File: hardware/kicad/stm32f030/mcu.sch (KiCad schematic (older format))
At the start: 13 parts, among them P10 SWD, P8 UART, P9 I2C, SW3 RESET, U2 STM32F030F4Px, Y1 8MHz

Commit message: hardware/kicad/stm32f030: progress
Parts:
- removed JP3: JP3x1, Pin_Headers:Pin_Header_Straight_1x03_Pitch2.54mm, symbol JP3x1
- added JP3: boot0, Pin_Headers:Pin_Header_Straight_1x02_Pitch2.54mm, symbol Jumper_NO_Small
- added R28: 10k, Resistors_SMD:R_0603_HandSoldering, symbol R_Small
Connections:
- net labels added: RXD, SWC, SWD, TXD
- wire segments 48 -> 53
- no-connect marks 0 -> 3
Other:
- moved on the sheet: C16, P10, P8, P9, R25, R26, SW3

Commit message: hardware/kicad/stm32f030: progress
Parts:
- U2: footprint Housings_SSOP:TSSOP-20_4.4x6.5mm_Pitch0.65mm -> Housings_SSOP:TSSOP-20_4.4x6.5mm_Pitch0.65mm_Handsoldering
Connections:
- net GND: now also SW3.1; no longer SW3.2
- net reset: now also SW3.2; no longer SW3.1
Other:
- moved on the sheet: C16
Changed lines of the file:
@@
 F 0 "U2" H 4450 4675 50  0000 L BNN
 F 1 "STM32F030F4Px" H 7650 4675 50  0000 R BNN
-F 2 "Housings_SSOP:TSSOP-20_4.4x6.5mm_Pitch0.65mm" H 7650 4625 50  0001 R TNN
+F 2 "Housings_SSOP:TSSOP-20_4.4x6.5mm_Pitch0.65mm_Handsoldering" H 7650 4625 50  0001 R TNN
 F 3 "" H 6050 3750 50  0000 C CNN
 	1    6050 3750
@@
 L +3.3V #PWR044
 U 1 1 5884CB05
-P 8800 4600
-F 0 "#PWR044" H 8800 4450 50  0001 C CNN
-F 1 "+3.3V" H 8800 4740 50  0000 C CNN
-F 2 "" H 8800 4600 50  0000 C CNN
-F 3 "" H 8800 4600 50  0000 C CNN
-	1    8800 4600
+P 8800 4500
+F 0 "#PWR044" H 8800 4350 50  0001 C CNN
+F 1 "+3.3V" H 8800 4640 50  0000 C CNN
+F 2 "" H 8800 4500 50  0000 C CNN
+F 3 "" H 8800 4500 50  0000 C CNN
+	1    8800 4500
 	1    0    0    -1
 $EndComp
@@
 L C_Small C16
 U 1 1 5884CB14
-P 8800 4750
-F 0 "C16" H 8810 4820 50  0000 L CNN
-F 1 "100n" H 8810 4670 50  0000 L CNN
-F 2 "Capacitors_SMD:C_0805_HandSoldering" H 8800 4750 50  0001 C CNN
-F 3 "" H 8800 4750 50  0000 C CNN
-	1    8800 4750
+P 8800 4700
+F 0 "C16" H 8810 4770 50  0000 L CNN
+F 1 "100n" H 8810 4620 50  0000 L CNN
+F 2 "Capacitors_SMD:C_0805_HandSoldering" H 8800 4700 50  0001 C CNN
+F 3 "" H 8800 4700 50  0000 C CNN
+	1    8800 4700
 	1    0    0    -1
 $EndComp
@@
 F 3 "" H 8600 3150 50  0000 C CNN
 	1    8600 3150
-	1    0    0    -1
+	-1   0    0    -1
 $EndComp
 $Comp
@@
 NoConn ~ 4350 3550
 Wire Wire Line
-	6050 2600 6050 2750
+	6050 2600 6050 2650
+Wire Wire Line
+	6050 2650 6050 2750
 Wire Wire Line
 	6150 2750 6150 2650
@@
 Connection ~ 6050 2650
 Wire Wire Line
-	6050 4650 6050 4900
-Wire Wire Line
-	8800 4600 8800 4650
-Wire Wire Line
-	8800 4850 8800 4900
+	8800 4500 8800 4600
+Wire Wire Line
+	8800 4800 8800 4900
 Wire Wire Line
 	7750 4250 9450 4250
 Wire Wire Line
-	7750 3150 8400 3150
-Wire Wire Line
-	8800 3150 8950 3150
+	7750 3150 7950 3150
+Wire Wire Line
+	7950 3150 8350 3150
+Wire Wire Line
+	8350 3150 8400 3150
 Wire Wire Line
 	8950 3150 8950 3250
 Wire Wire Line
-	7950 2950 7950 4150
+	7950 2950 7950 3150
+Wire Wire Line
+	7950 3150 7950 4150
 Connection ~ 7950 3150
 Wire Wire Line
 	7950 2600 7950 2750
 Wire Wire Line
-	3950 3550 3950 4900
+	3950 3550 3950 3950
+Wire Wire Line
+	3950 3950 3950 4600
+Wire Wire Line
+	3950 4600 3950 4900
 Wire Wire Line
 	3950 4600 3900 4600
@@
 	3900 3550 3950 3550
 Wire Wire Line
-	7850 4050 7850 4600
+	7850 4050 7850 4450
+Wire Wire Line
+	7850 4450 7850 4600
 Wire Wire Line
 	7850 4050 7750 4050
 Wire Wire Line
-	8150 3950 8150 4600
+	8150 3950 8150 4450
+Wire Wire Line
+	8150 4450 8150 4600
 Wire Wire Line
 	8150 3950 7750 3950
@@
 	3050 3000 4250 3000
 Wire Wire Line
-	4250 2850 4250 4050
-Wire Wire Line
-	4050 2850 4050 4050
+	4250 2850 4250 3000
+Wire Wire Line
+	4250 3000 4250 4050
+Wire Wire Line
+	4050 2850 4050 3100
+Wire Wire Line
+	4050 3100 4050 3950
+Wire Wire Line
+	4050 3950 4050 4050
 Connection ~ 4050 3100
 Connection ~ 4250 3000
@@
 	4050 4050 3900 4050
 Wire Wire Line
-	4150 4050 4350 4050
+	4150 4050 4250 4050
+Wire Wire Line
+	4250 4050 4350 4050
 Wire Wire Line
 	4150 4050 4150 4150
@@
 	8550 3750 8550 4300
 Wire Wire Line
-	8550 4500 8550 4600
+	8550 4500 8550 4550
+Wire Wire Line
+	8550 4550 8550 4600
 Wire Wire Line
 	8550 4900 8550 4800
@@
 Text Label 4000 4500 0    60   ~ 0
 SWD
+Wire Wire Line
+	8800 3150 8850 3150
+Wire Wire Line
+	8850 3150 8950 3150
+Wire Wire Line
+	8400 3250 8350 3250
+Wire Wire Line
+	8350 3250 8350 3150
+Connection ~ 8350 3150
+Wire Wire Line
+	8800 3250 8850 3250
+Wire Wire Line
+	8850 3250 8850 3150
+Connection ~ 8850 3150
+Wire Wire Line
+	6050 4900 6050 4650
 $EndSCHEMATC

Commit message: hardware/kicad/stm32f030: modules ready
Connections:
- net RXD: now also P8.1 (P1); no longer P8.2 (P2)
- net TXD: now also P8.2 (P2); no longer P8.1 (P1)
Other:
- moved on the sheet: P8
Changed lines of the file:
@@
 L CONN_01X03 P8
 U 1 1 5884E804
-P 3700 3450
-F 0 "P8" H 3700 3650 50  0000 C CNN
-F 1 "UART" V 3800 3450 50  0000 C CNN
-F 2 "Pin_Headers:Pin_Header_Straight_1x03_Pitch2.54mm" H 3700 3450 50  0001 C CNN
-F 3 "" H 3700 3450 50  0000 C CNN
-	1    3700 3450
-	-1   0    0    -1
+P 3700 3350
+F 0 "P8" H 3700 3550 50  0000 C CNN
+F 1 "UART" V 3800 3350 50  0000 C CNN
+F 2 "Pin_Headers:Pin_Header_Straight_1x03_Pitch2.54mm" H 3700 3350 50  0001 C CNN
+F 3 "" H 3700 3350 50  0000 C CNN
+	1    3700 3350
+	-1   0    0    1
 $EndComp
 Text HLabel 3050 3100 0    60   Output ~ 0
@@
 NoConn ~ 4350 3250
 NoConn ~ 4350 3550
-Wire Wire Line
-	6050 2600 6050 2650
-Wire Wire Line
-	6050 2650 6050 2750
-Wire Wire Line
-	6150 2750 6150 2650
-Wire Wire Line
-	6150 2650 6050 2650
-Connection ~ 6050 2650
-Wire Wire Line
-	8800 4500 8800 4600
-Wire Wire Line
-	8800 4800 8800 4900
-Wire Wire Line
-	7750 4250 9450 4250
-Wire Wire Line
-	7750 3150 7950 3150
-Wire Wire Line
-	7950 3150 8350 3150
-Wire Wire Line
-	8350 3150 8400 3150
-Wire Wire Line
-	8950 3150 8950 3250
-Wire Wire Line
-	7950 2950 7950 3150
-Wire Wire Line
-	7950 3150 7950 4150
-Connection ~ 7950 3150
-Wire Wire Line
-	7950 2600 7950 2750
-Wire Wire Line
-	3950 3550 3950 3950
-Wire Wire Line
-	3950 3950 3950 4600
-Wire Wire Line
-	3950 4600 3950 4900
-Wire Wire Line
-	3950 4600 3900 4600
-Connection ~ 3950 4600
-Wire Wire Line
-	3900 3550 3950 3550
-Wire Wire Line
-	7850 4050 7850 4450
-Wire Wire Line
-	7850 4450 7850 4600
-Wire Wire Line
-	7850 4050 7750 4050
-Wire Wire Line
-	8150 3950 8150 4450
-Wire Wire Line
-	8150 4450 8150 4600
-Wire Wire Line
-	8150 3950 7750 3950
-Wire Wire Line
-	7900 4450 7850 4450
-Connection ~ 7850 4450
-Wire Wire Line
-	8100 4450 8150 4450
-Connection ~ 8150 4450
-Wire Wire Line
-	8150 4900 8150 4800
-Wire Wire Line
-	7850 4900 7850 4800
-Wire Wire Line
-	4250 4150 4350 4150
-Wire Wire Line
-	4300 4250 4350 4250
-Wire Wire Line
-	3050 3850 4350 3850
-Wire Wire Line
-	3050 3750 4350 3750
-Wire Wire Line
-	3050 3650 4350 3650
-Wire Wire Line
-	3900 3450 4350 3450
-Wire Wire Line
-	3900 3350 4350 3350
-Wire Wire Line
-	7950 4150 9450 4150
-Wire Wire Line
-	3050 3100 4050 3100
-Connection ~ 4050 3950
-Wire Wire Line
-	3050 3000 4250 3000
-Wire Wire Line
-	4250 2850 4250 3000
-Wire Wire Line
-	4250 3000 4250 4050
-Wire Wire Line
-	4050 2850 4050 3100
-Wire Wire Line
-	4050 3100 4050 3950
-Wire Wire Line
-	4050 3950 4050 4050
-Connection ~ 4050 3100
-Connection ~ 4250 3000
-Wire Wire Line
-	4050 2600 4050 2650
-Wire Wire Line
-	4250 2600 4250 2650
-Wire Wire Line
-	4250 4150 4250 4500
-Wire Wire Line
-	4250 4500 3900 4500
-Wire Wire Line
-	3900 4400 4300 4400
-Wire Wire Line
-	4300 4400 4300 4250
-Wire Wire Line
-	4050 3950 4350 3950
-Wire Wire Line
-	3900 3950 3950 3950
-Connection ~ 3950 3950
-Wire Wire Line
-	4050 4050 3900 4050
-Wire Wire Line
-	4150 4050 4250 4050
-Wire Wire Line
-	4250 4050 4350 4050
-Wire Wire Line
-	4150 4050 4150 4150
-Wire Wire Line
-	4150 4150 3900 4150
-Connection ~ 4250 4050
 $Comp
 L R_Small R28
@@
 	0    1    1    0
 $EndComp
-Wire Wire Line
-	8550 3750 8550 4300
-Wire Wire Line
-	8550 4500 8550 4550
-Wire Wire Line
-	8550 4550 8550 4600
-Wire Wire Line
-	8550 4900 8550 4800
-Wire Wire Line
-	8550 4550 8350 4550
-Wire Wire Line
-	8350 4550 8350 3350
-Wire Wire Line
-	8350 3350 7750 3350
-Connection ~ 8550 4550
-Text Label 3950 3350 0    60   ~ 0
-TXD
-Text Label 3950 3450 0    60   ~ 0
+Text Label 4000 3450 0    60   ~ 0
 RXD
 Text Label 4000 4400 0    60   ~ 0
@@
 SWD
 Wire Wire Line
-	8800 3150 8850 3150
-Wire Wire Line
-	8850 3150 8950 3150
+	6050 2600 6050 2750
+Wire Wire Line
+	6150 2750 6150 2650
+Wire Wire Line
+	6150 2650 6050 2650
+Connection ~ 6050 2650
+Wire Wire Line
+	8800 4500 8800 4600
+Wire Wire Line
+	8800 4800 8800 4900
+Wire Wire Line
+	7750 4250 9450 4250
+Wire Wire Line
+	7750 3150 8400 3150
+Wire Wire Line
+	8950 3150 8950 3250
+Wire Wire Line
+	7950 2950 7950 4150
+Connection ~ 7950 3150
+Wire Wire Line
+	7950 2600 7950 2750
+Wire Wire Line
+	3950 4600 3900 4600
+Connection ~ 3950 4600
+Wire Wire Line
+	7850 4050 7850 4600
+Wire Wire Line
+	7850 4050 7750 4050
+Wire Wire Line
+	8150 3950 8150 4600
+Wire Wire Line
+	8150 3950 7750 3950
+Wire Wire Line
+	7900 4450 7850 4450
+Connection ~ 7850 4450
+Wire Wire Line
+	8100 4450 8150 4450
+Connection ~ 8150 4450
+Wire Wire Line
+	8150 4900 8150 4800
+Wire Wire Line
+	7850 4900 7850 4800
+Wire Wire Line
+	4250 4150 4350 4150
+Wire Wire Line
+	4300 4250 4350 4250
+Wire Wire Line
+	3050 3850 4350 3850
+Wire Wire Line
+	3050 3750 4350 3750
+Wire Wire Line
+	3050 3650 4350 3650
+Wire Wire Line
+	7950 4150 9450 4150
+Wire Wire Line
+	3050 3100 4050 3100
+Connection ~ 4050 3950
+Wire Wire Line
+	3050 3000 4250 3000
+Wire Wire Line
+	4250 2850 4250 4050
+Wire Wire Line
+	4050 2850 4050 4050
+Connection ~ 4050 3100
+Connection ~ 4250 3000
+Wire Wire Line
+	4050 2600 4050 2650
+Wire Wire Line
+	4250 2600 4250 2650
+Wire Wire Line
+	4250 4150 4250 4500
+Wire Wire Line
+	4250 4500 3900 4500
+Wire Wire Line
+	3900 4400 4300 4400
+Wire Wire Line
+	4300 4400 4300 4250
+Wire Wire Line
+	4050 3950 4350 3950
+Wire Wire Line
+	3900 3950 3950 3950
+Connection ~ 3950 3950
+Wire Wire Line
+	4050 4050 3900 4050
+Wire Wire Line
+	4150 4050 4350 4050
+Wire Wire Line
+	4150 4050 4150 4150
+Wire Wire Line
+	4150 4150 3900 4150
+Connection ~ 4250 4050
+Wire Wire Line
+	8550 3750 8550 4300
+Wire Wire Line
+	8550 4500 8550 4600
+Wire Wire Line
+	8550 4900 8550 4800
+Wire Wire Line
+	8550 4550 8350 4550
+Wire Wire Line
+	8350 4550 8350 3350
+Wire Wire Line
+	8350 3350 7750 3350
+Connection ~ 8550 4550
+Wire Wire Line
+	8800 3150 8950 3150
 Wire Wire Line
 	8400 3250 8350 3250
@@
 Wire Wire Line
 	6050 4900 6050 4650
+Wire Wire Line
+	3900 3350 4350 3350
+Wire Wire Line
+	3950 3250 3950 4900
+Wire Wire Line
+	3200 4750 3950 4750
+Connection ~ 3950 4750
+Wire Wire Line
+	3950 3250 3900 3250
+Wire Wire Line
+	3900 3450 4350 3450
+Text Label 4000 3350 0    60   ~ 0
+TXD
 $EndSCHEMATC

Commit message: PCB V0.90
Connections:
- net SWC: now also P10.2 (P2); no longer P10.1 (P1)
- net SWD: now also P10.1 (P1); no longer P10.2 (P2)
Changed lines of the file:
@@
 Text Label 4000 3450 0    60   ~ 0
 RXD
+Text Label 4000 4500 0    60   ~ 0
+SWC
 Text Label 4000 4400 0    60   ~ 0
-SWC
-Text Label 4000 4500 0    60   ~ 0
 SWD
 Wire Wire Line
@@
 	7850 4900 7850 4800
 Wire Wire Line
-	4250 4150 4350 4150
-Wire Wire Line
 	4300 4250 4350 4250
 Wire Wire Line
@@
 Wire Wire Line
 	4250 2600 4250 2650
-Wire Wire Line
-	4250 4150 4250 4500
-Wire Wire Line
-	4250 4500 3900 4500
-Wire Wire Line
-	3900 4400 4300 4400
-Wire Wire Line
-	4300 4400 4300 4250
 Wire Wire Line
 	4050 3950 4350 3950
@@
 Text Label 4000 3350 0    60   ~ 0
 TXD
+Wire Wire Line
+	4350 4150 4250 4150
+Wire Wire Line
+	4250 4150 4250 4400
+Wire Wire Line
+	4250 4400 3900 4400
+Wire Wire Line
+	4300 4250 4300 4500
+Wire Wire Line
+	4300 4500 3900 4500
 $EndSCHEMATC

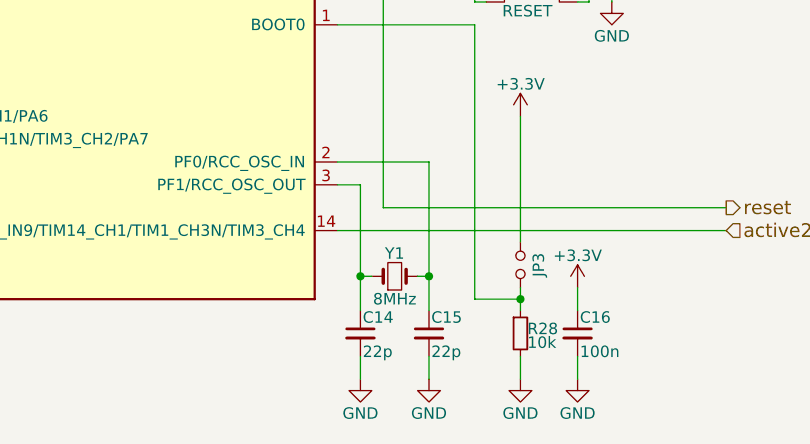
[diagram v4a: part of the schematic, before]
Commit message: hardware/kicad/stm32f030: adding eeprom step1
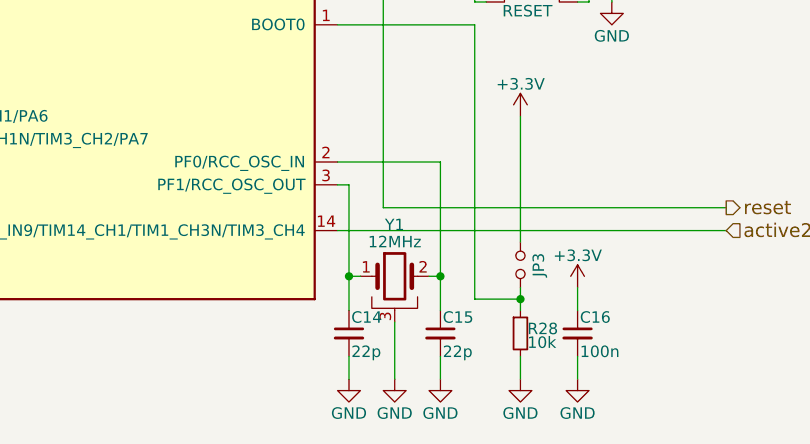
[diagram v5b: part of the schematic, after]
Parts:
- removed Y1: 8MHz, Crystals:Crystal_HC49-SD_SMD, symbol Crystal_Small
- added Y1: 12MHz, Crystals:Crystal_SMD_3225_4Pads, symbol Crystal_GND3
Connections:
- net GND: now also Y1.3
- net at C15.1, U2.2 (PF0/RCC_OSC_IN): now also Y1.2
- net at C14.1, U2.3 (PF1/RCC_OSC_OUT): now also Y1.1
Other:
- moved on the sheet: C14, C15
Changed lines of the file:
@@
 $Descr A4 11693 8268
 encoding utf-8
-Sheet 5 5
+Sheet 5 6
 Title ""
 Date ""
@@
 $EndComp
 $Comp
-L +3.3V #PWR041
+L +3.3V #PWR43
 U 1 1 5884CABB
 P 6050 2600
-F 0 "#PWR041" H 6050 2450 50  0001 C CNN
+F 0 "#PWR43" H 6050 2450 50  0001 C CNN
 F 1 "+3.3V" H 6050 2740 50  0000 C CNN
 F 2 "" H 6050 2600 50  0000 C CNN
@@
 $EndComp
 $Comp
-L GND #PWR042
+L GND #PWR49
 U 1 1 5884CAD9
 P 6050 4900
-F 0 "#PWR042" H 6050 4650 50  0001 C CNN
+F 0 "#PWR49" H 6050 4650 50  0001 C CNN
 F 1 "GND" H 6050 4750 50  0000 C CNN
 F 2 "" H 6050 4900 50  0000 C CNN
@@
 $EndComp
 $Comp
-L GND #PWR043
+L GND #PWR54
 U 1 1 5884CAF5
 P 8800 4900
-F 0 "#PWR043" H 8800 4650 50  0001 C CNN
+F 0 "#PWR54" H 8800 4650 50  0001 C CNN
 F 1 "GND" H 8800 4750 50  0000 C CNN
 F 2 "" H 8800 4900 50  0000 C CNN
@@
 $EndComp
 $Comp
-L +3.3V #PWR044
+L +3.3V #PWR47
 U 1 1 5884CB05
 P 8800 4500
-F 0 "#PWR044" H 8800 4350 50  0001 C CNN
+F 0 "#PWR47" H 8800 4350 50  0001 C CNN
 F 1 "+3.3V" H 8800 4640 50  0000 C CNN
 F 2 "" H 8800 4500 50  0000 C CNN
@@
 osc2
 $Comp
-L Crystal_Small Y1
-U 1 1 5884DD83
-P 8000 4450
-F 0 "Y1" H 8000 4550 50  0000 C CNN
-F 1 "8MHz" H 8000 4350 50  0000 C CNN
-F 2 "Crystals:Crystal_HC49-SD_SMD" H 8000 4450 50  0001 C CNN
-F 3 "" H 8000 4450 50  0000 C CNN
-	1    8000 4450
-	1    0    0    -1
-$EndComp
-$Comp
 L C_Small C15
 U 1 1 5884DE3A
-P 8150 4700
-F 0 "C15" H 8160 4770 50  0000 L CNN
-F 1 "22p" H 8160 4620 50  0000 L CNN
-F 2 "Capacitors_SMD:C_0603_HandSoldering" H 8150 4700 50  0001 C CNN
-F 3 "" H 8150 4700 50  0000 C CNN
-	1    8150 4700
+P 8200 4700
+F 0 "C15" H 8210 4770 50  0000 L CNN
+F 1 "22p" H 8210 4620 50  0000 L CNN
+F 2 "Capacitors_SMD:C_0603_HandSoldering" H 8200 4700 50  0001 C CNN
+F 3 "" H 8200 4700 50  0000 C CNN
+	1    8200 4700
 	1    0    0    -1
 $EndComp
@@
 L C_Small C14
 U 1 1 5884DE87
-P 7850 4700
-F 0 "C14" H 7860 4770 50  0000 L CNN
-F 1 "22p" H 7860 4620 50  0000 L CNN
-F 2 "Capacitors_SMD:C_0603_HandSoldering" H 7850 4700 50  0001 C CNN
-F 3 "" H 7850 4700 50  0000 C CNN
-	1    7850 4700
-	1    0    0    -1
-$EndComp
-$Comp
-L GND #PWR045
+P 7800 4700
+F 0 "C14" H 7810 4770 50  0000 L CNN
+F 1 "22p" H 7810 4620 50  0000 L CNN
+F 2 "Capacitors_SMD:C_0603_HandSoldering" H 7800 4700 50  0001 C CNN
+F 3 "" H 7800 4700 50  0000 C CNN
+	1    7800 4700
+	1    0    0    -1
+$EndComp
+$Comp
+L GND #PWR50
 U 1 1 5884DEF5
-P 7850 4900
-F 0 "#PWR045" H 7850 4650 50  0001 C CNN
-F 1 "GND" H 7850 4750 50  0000 C CNN
-F 2 "" H 7850 4900 50  0000 C CNN
-F 3 "" H 7850 4900 50  0000 C CNN
-	1    7850 4900
-	1    0    0    -1
-$EndComp
-$Comp
-L GND #PWR046
+P 7800 4900
+F 0 "#PWR50" H 7800 4650 50  0001 C CNN
+F 1 "GND" H 7800 4750 50  0000 C CNN
+F 2 "" H 7800 4900 50  0000 C CNN
+F 3 "" H 7800 4900 50  0000 C CNN
+	1    7800 4900
+	1    0    0    -1
+$EndComp
+$Comp
+L GND #PWR52
 U 1 1 5884DF18
-P 8150 4900
-F 0 "#PWR046" H 8150 4650 50  0001 C CNN
-F 1 "GND" H 8150 4750 50  0000 C CNN
-F 2 "" H 8150 4900 50  0000 C CNN
-F 3 "" H 8150 4900 50  0000 C CNN
-	1    8150 4900
-	1    0    0    -1
-$EndComp
-$Comp
-L GND #PWR047
+P 8200 4900
+F 0 "#PWR52" H 8200 4650 50  0001 C CNN
+F 1 "GND" H 8200 4750 50  0000 C CNN
+F 2 "" H 8200 4900 50  0000 C CNN
+F 3 "" H 8200 4900 50  0000 C CNN
+	1    8200 4900
+	1    0    0    -1
+$EndComp
+$Comp
+L GND #PWR53
 U 1 1 5884DF65
 P 8550 4900
-F 0 "#PWR047" H 8550 4650 50  0001 C CNN
+F 0 "#PWR53" H 8550 4650 50  0001 C CNN
 F 1 "GND" H 8550 4750 50  0000 C CNN
 F 2 "" H 8550 4900 50  0000 C CNN
@@
 $EndComp
 $Comp
-L GND #PWR048
+L GND #PWR45
 U 1 1 5884E164
 P 8950 3250
-F 0 "#PWR048" H 8950 3000 50  0001 C CNN
+F 0 "#PWR45" H 8950 3000 50  0001 C CNN
 F 1 "GND" H 8950 3100 50  0000 C CNN
 F 2 "" H 8950 3250 50  0000 C CNN
@@
 $EndComp
 $Comp
-L +3.3V #PWR049
+L +3.3V #PWR44
 U 1 1 5884E1FE
 P 7950 2600
-F 0 "#PWR049" H 7950 2450 50  0001 C CNN
+F 0 "#PWR44" H 7950 2450 50  0001 C CNN
 F 1 "+3.3V" H 7950 2740 50  0000 C CNN
 F 2 "" H 7950 2600 50  0000 C CNN
@@
 $EndComp
 $Comp
-L GND #PWR050
+L GND #PWR48
 U 1 1 5884E75E
 P 3950 4900
-F 0 "#PWR050" H 3950 4650 50  0001 C CNN
+F 0 "#PWR48" H 3950 4650 50  0001 C CNN
 F 1 "GND" H 3950 4750 50  0000 C CNN
 F 2 "" H 3950 4900 50  0000 C CNN
@@
 $EndComp
 $Comp
-L +3.3V #PWR051
+L +3.3V #PWR41
 U 1 1 58855640
 P 4050 2600
-F 0 "#PWR051" H 4050 2450 50  0001 C CNN
+F 0 "#PWR41" H 4050 2450 50  0001 C CNN
 F 1 "+3.3V" H 4050 2740 50  0000 C CNN
 F 2 "" H 4050 2600 50  0000 C CNN
@@
 $EndComp
 $Comp
-L +3.3V #PWR052
+L +3.3V #PWR42
 U 1 1 5885566F
 P 4250 2600
-F 0 "#PWR052" H 4250 2450 50  0001 C CNN
+F 0 "#PWR42" H 4250 2450 50  0001 C CNN
 F 1 "+3.3V" H 4250 2740 50  0000 C CNN
 F 2 "" H 4250 2600 50  0000 C CNN
@@
 $EndComp
 $Comp
-L +3.3V #PWR053
+L +3.3V #PWR46
 U 1 1 5885595B
 P 8550 3750
-F 0 "#PWR053" H 8550 3600 50  0001 C CNN
+F 0 "#PWR46" H 8550 3600 50  0001 C CNN
 F 1 "+3.3V" H 8550 3890 50  0000 C CNN
 F 2 "" H 8550 3750 50  0000 C CNN
@@
 Connection ~ 3950 4600
 Wire Wire Line
-	7850 4050 7850 4600
-Wire Wire Line
-	7850 4050 7750 4050
-Wire Wire Line
-	8150 3950 8150 4600
-Wire Wire Line
-	8150 3950 7750 3950
-Wire Wire Line
-	7900 4450 7850 4450
-Connection ~ 7850 4450
-Wire Wire Line
-	8100 4450 8150 4450
-Connection ~ 8150 4450
-Wire Wire Line
-	8150 4900 8150 4800
-Wire Wire Line
-	7850 4900 7850 4800
+	7800 4050 7800 4600
+Wire Wire Line
+	7800 4050 7750 4050
+Wire Wire Line
+	8200 3950 8200 4600
+Wire Wire Line
+	8200 3950 7750 3950
+Wire Wire Line
+	8200 4900 8200 4800
+Wire Wire Line
+	7800 4900 7800 4800
 Wire Wire Line
 	4300 4250 4350 4250
@@
 Wire Wire Line
 	4300 4500 3900 4500
+$Comp
+L Crystal_GND3 Y1
+U 1 1 5895F20E
+P 8000 4450
+F 0 "Y1" H 8000 4675 50  0000 C CNN
+F 1 "12MHz" H 8000 4600 50  0000 C CNN
+F 2 "Crystals:Crystal_SMD_3225_4Pads" H 8000 4450 50  0001 C CNN
+F 3 "" H 8000 4450 50  0000 C CNN
+	1    8000 4450
+	1    0    0    -1
+$EndComp
+$Comp
+L GND #PWR51
+U 1 1 5895F412
+P 8000 4900
+F 0 "#PWR51" H 8000 4650 50  0001 C CNN
+F 1 "GND" H 8000 4750 50  0000 C CNN
+F 2 "" H 8000 4900 50  0000 C CNN
+F 3 "" H 8000 4900 50  0000 C CNN
+	1    8000 4900
+	1    0    0    -1
+$EndComp
+Wire Wire Line
+	8000 4900 8000 4650
+Wire Wire Line
+	8150 4450 8200 4450
+Connection ~ 8200 4450
+Wire Wire Line
+	7850 4450 7800 4450
+Connection ~ 7800 4450
 $EndSCHEMATC

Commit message: hardware/kicad/stm32f030: blocks ready
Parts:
- removed Y1: 12MHz, Crystals:Crystal_SMD_3225_4Pads, symbol Crystal_GND3
- added Y1: 8MHz, Crystals:Crystal_HC49-4H_Vertical, symbol Crystal_Small
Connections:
- net at C15.1, U2.2 (PF0/RCC_OSC_IN): now also Y1.2
- net at C14.1, U2.3 (PF1/RCC_OSC_OUT): now also Y1.1
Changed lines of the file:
@@
 $Descr A4 11693 8268
 encoding utf-8
-Sheet 5 6
+Sheet 4 5
 Title ""
 Date ""
@@
 	8800 4800 8800 4900
 Wire Wire Line
-	7750 4250 9450 4250
-Wire Wire Line
 	7750 3150 8400 3150
 Wire Wire Line
@@
 	3950 3250 3950 4900
 Wire Wire Line
-	3200 4750 3950 4750
-Connection ~ 3950 4750
-Wire Wire Line
 	3950 3250 3900 3250
 Wire Wire Line
@@
 Wire Wire Line
 	4300 4500 3900 4500
-$Comp
-L Crystal_GND3 Y1
-U 1 1 5895F20E
+Wire Wire Line
+	8100 4450 8200 4450
+Connection ~ 8200 4450
+Wire Wire Line
+	7900 4450 7800 4450
+Connection ~ 7800 4450
+Wire Wire Line
+	7750 4250 9450 4250
+$Comp
+L Crystal_Small Y1
+U 1 1 58B1F379
 P 8000 4450
-F 0 "Y1" H 8000 4675 50  0000 C CNN
-F 1 "12MHz" H 8000 4600 50  0000 C CNN
-F 2 "Crystals:Crystal_SMD_3225_4Pads" H 8000 4450 50  0001 C CNN
+F 0 "Y1" H 8000 4550 50  0000 C CNN
+F 1 "8MHz" H 8000 4350 50  0000 C CNN
+F 2 "Crystals:Crystal_HC49-4H_Vertical" H 8000 4450 50  0001 C CNN
 F 3 "" H 8000 4450 50  0000 C CNN
 	1    8000 4450
 	1    0    0    -1
 $EndComp
-$Comp
-L GND #PWR045
-U 1 1 5895F412
-P 8000 4900
-F 0 "#PWR045" H 8000 4650 50  0001 C CNN
-F 1 "GND" H 8000 4750 50  0000 C CNN
-F 2 "" H 8000 4900 50  0000 C CNN
-F 3 "" H 8000 4900 50  0000 C CNN
-	1    8000 4900
-	1    0    0    -1
-$EndComp
-Wire Wire Line
-	8000 4900 8000 4650
-Wire Wire Line
-	8150 4450 8200 4450
-Connection ~ 8200 4450
-Wire Wire Line
-	7850 4450 7800 4450
-Connection ~ 7800 4450
 $EndSCHEMATC
